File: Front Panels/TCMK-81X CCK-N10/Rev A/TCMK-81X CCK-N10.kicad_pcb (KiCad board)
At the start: 2 copper layers, 107.1 x 26.9 mm, 6 parts, among them U1 11 Pin FFC Connector, U2 Controller Port, U3 Controller Port

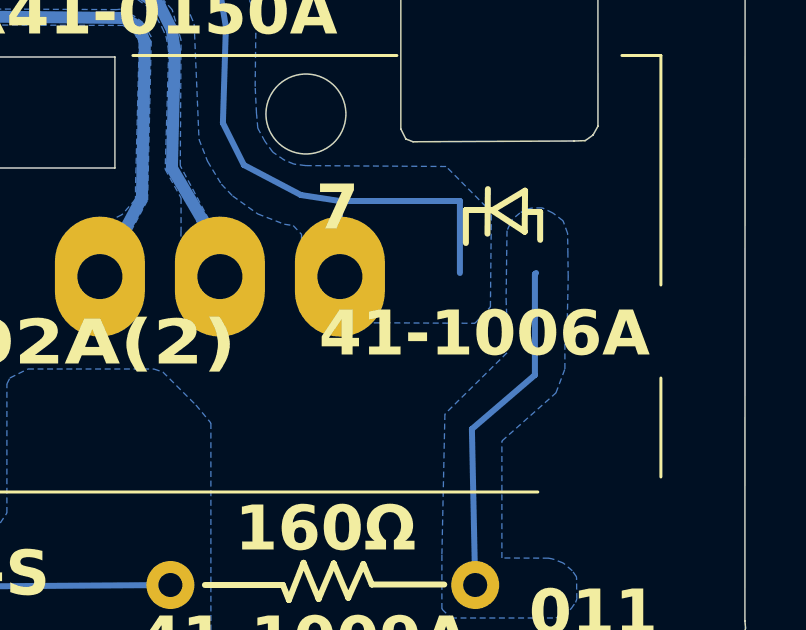
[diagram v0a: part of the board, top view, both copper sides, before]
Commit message: Fix Issue #4: SFC Controller Board LED Footprint
This is embarassing and I'm not sure how it happened, but somehow
the LED footprint went missing. I have no idea what happened here
and apologize profusely to anyone affected.

The footprint was still there in the schema but became unlinked
from the board and raised a DRC issue. I have corrected this now
and will investigate to see if I can find out what happened.
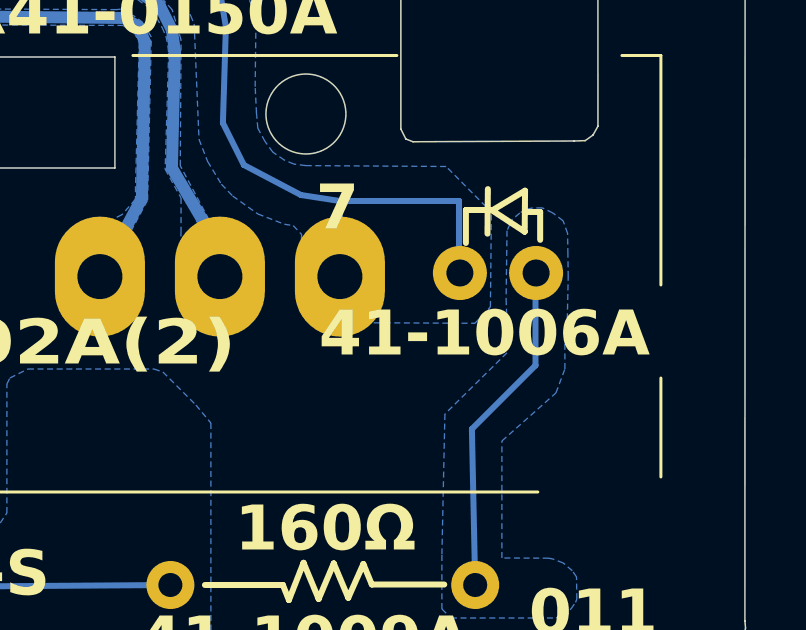
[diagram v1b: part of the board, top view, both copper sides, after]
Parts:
- added D1: LED, LED_THT:LED_D1.8mm_W1.8mm_H2.4mm_Horizontal_O6.35mm_Z1.6mm, B.Cu at (155.0, 61.6)
- U1: value 11 Pin FFC Connector -> ~
- U2, U3: value Controller Port -> ~
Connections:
- U1 pad 10: 8 -> 10
- U1 pad 8: 6 -> 8
- U2 pad 3: 8 -> 10
- U3 pad 2: 6 -> 8
- U3 pad 3: 8 -> 10
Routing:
- net 10: track 0.00 -> 72.6 mm, vias 0 -> 4
- net 6: track 40.2 -> 0.00 mm, vias 4 -> 0
- net 8: track 72.6 -> 40.2 mm
- added copper zone on B.Cu, net 10
- added copper zone on F.Cu, net 8
- removed copper zone on B.Cu, net 6
- removed copper zone on F.Cu, net 6
